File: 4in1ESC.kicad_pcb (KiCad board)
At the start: 6 copper layers, 31.2 x 33 mm, 197 parts, among them J1 SM08B-SRSS-TB, Q1 SP40N03GNJ, Q10 SP40N03GNJ, Q11 SP40N03GNJ, Q12 SP40N03GNJ, Q13 SP40N03GNJ, Q14 SP40N03GNJ, Q15 SP40N03GNJ, Q16 SP40N03GNJ, Q17 SP40N03GNJ, Q18 SP40N03GNJ, Q19 SP40N03GNJ, Q2 SP40N03GNJ, Q20 SP40N03GNJ, Q21 SP40N03GNJ, Q22 SP40N03GNJ, Q23 SP40N03GNJ, Q24 SP40N03GNJ, Q3 SP40N03GNJ, Q4 SP40N03GNJ, Q5 SP40N03GNJ, Q6 SP40N03GNJ, Q7 SP40N03GNJ, Q8 SP40N03GNJ, Q9 SP40N03GNJ, U1 TLV76733DRVR, U10 AT32F421G8U7, U11 NSG2065Q, U12 INA186A3IDCKR, U18 LMR51420YDDCR, U2 AT32F421G8U7, U3 NSG2065Q, U5 XRIM160808SR47MBCD, U6 AT32F421G8U7, U7 NSG2065Q, U8 AT32F421G8U7, U9 NSG2065Q

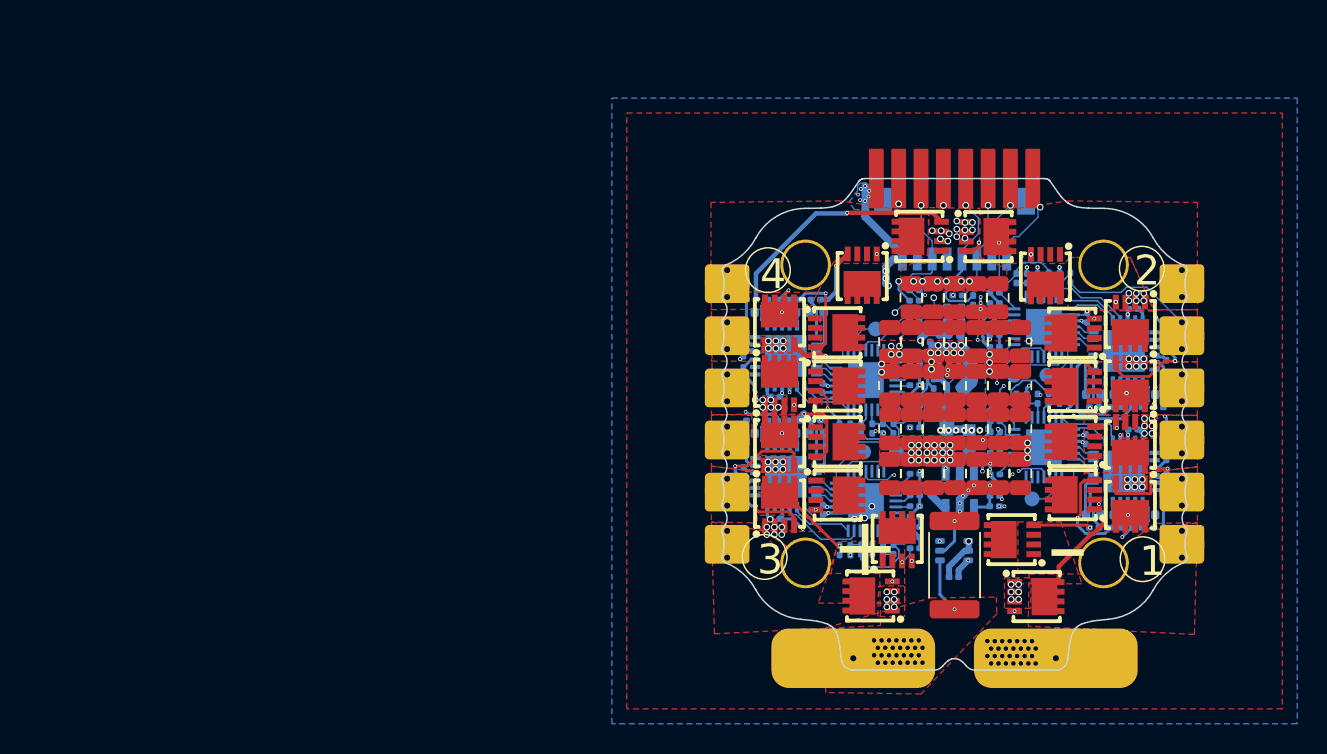
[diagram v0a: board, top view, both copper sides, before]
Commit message: V-beta schematic in progress: buck/inductor/TVS/MOSFET swaps
Stan's V-beta edits via KiCad GUI:
- U13 LMR54406DBVR placed (replacing LMR51420)
- R119 = 115k for 10V output (Vfb=0.8V)
- U5 inductor value updated to FTC160808S4R7MBCA (4.7uH)
- D1 SMF24A-T13 TVS placed across +BATT/GND
- 24x SP40N03GNJ -> DOY180N03T (TDFN3333-8PL)
- 14x bulk caps in 1206 (replacing the 0805 swarm)
- R74 = 10R 0201 added between VDD and VDDA (no ferrite)
- Ferrites FB1-4 removed
- LMR54406 footprint and 3D imported via easyeda2kicad
- SMF24A-T13 footprint and 3D imported via easyeda2kicad

Schematic still has hygiene issues (footprint namespace prefixes,
cap/resistor R/C footprint swaps) to fix in a follow-up.

Generator version bumped to KiCad 10.0 (was 9.x).

Co-Authored-By: Claude Opus 4.7 (1M context) <noreply@anthropic.com>
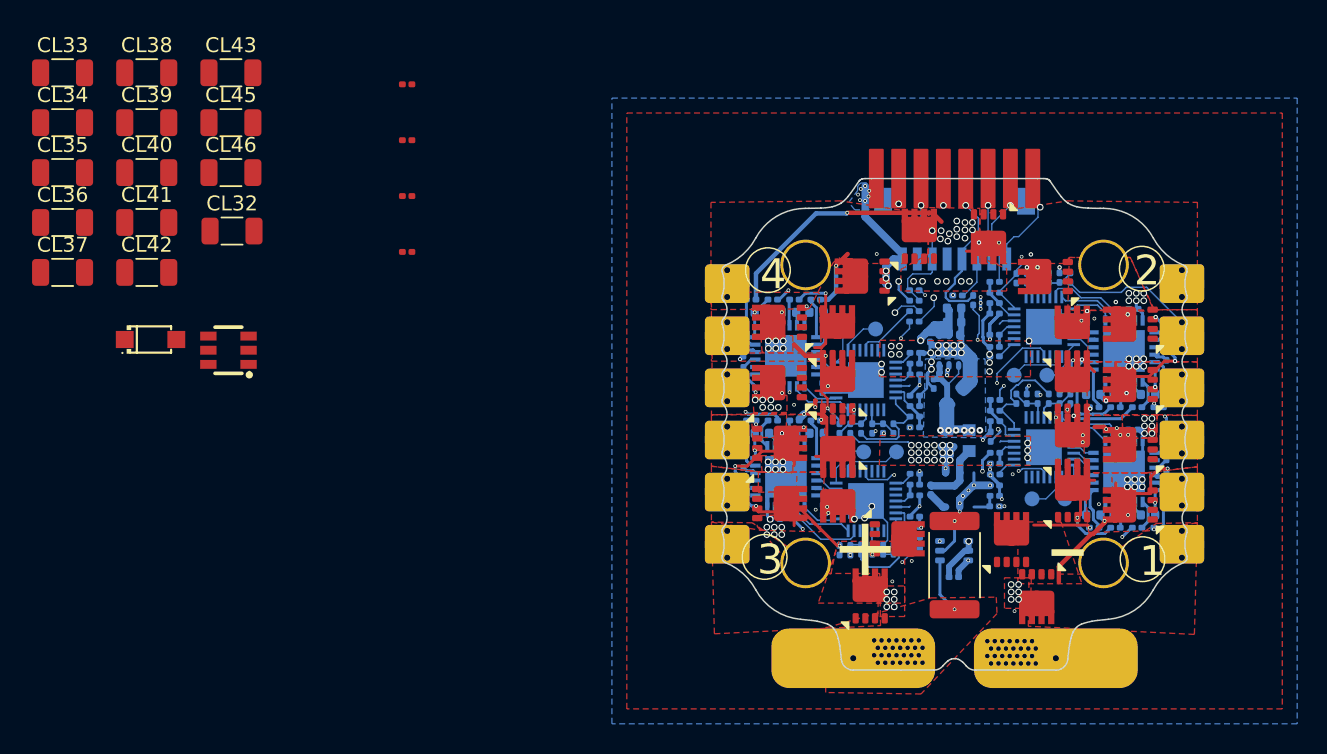
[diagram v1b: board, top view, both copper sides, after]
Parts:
- removed C10, C11, C12, C13, C14, C15, C16, C17, C18, C19, C2, C20, C21, C22, C23, C24, C25, C26, C27, C28, C29, C3, C31, C4, C40, C41, C47, C5, C51, C6, C7, C8, C9: 10uF, Capacitor_SMD:C_0805_2012Metric
- removed FB1, FB2, FB3, FB4: BLM03HD331SN1D, Inductor_SMD:L_0201_0603Metric
- removed U18: LMR51420YDDCR, components:SOT-23-6_L2.9-W1.6-P0.95-LS2.9-BL
- added CL32: 10uF, Capacitor_SMD:C_1206_3216Metric, F.Cu at (27.5, 35.9)
- added CL33: 10uF, Capacitor_SMD:C_1206_3216Metric, F.Cu at (16.1, 25.3)
- added CL34: 10uF, Capacitor_SMD:C_1206_3216Metric, F.Cu at (16.1, 28.6)
- added CL35: 10uF, Capacitor_SMD:C_1206_3216Metric, F.Cu at (16.1, 32.0)
- added CL36: 10uF, Capacitor_SMD:C_1206_3216Metric, F.Cu at (16.1, 35.4)
- added CL37: 10uF, Capacitor_SMD:C_1206_3216Metric, F.Cu at (16.1, 38.7)
- added CL38: 10uF, Capacitor_SMD:C_1206_3216Metric, F.Cu at (21.8, 25.3)
- added CL39: 10uF, Capacitor_SMD:C_1206_3216Metric, F.Cu at (21.8, 28.6)
- added CL40: 10uF, Capacitor_SMD:C_1206_3216Metric, F.Cu at (21.8, 32.0)
- added CL41: 10uF, Capacitor_SMD:C_1206_3216Metric, F.Cu at (21.8, 35.4)
- added CL42: 10uF, Capacitor_SMD:C_1206_3216Metric, F.Cu at (21.8, 38.7)
- added CL43: 10uF, Capacitor_SMD:C_1206_3216Metric, F.Cu at (27.4, 25.3)
- added CL45: 10uF, Capacitor_SMD:C_1206_3216Metric, F.Cu at (27.4, 28.6)
- added CL46: 10uF, Capacitor_SMD:C_1206_3216Metric, F.Cu at (27.4, 32.0)
- added D1: SMF24A-T13, 4in1ESC:SOD-123FL_L2.7-W1.8-LS3.7-RD, F.Cu at (22.0, 43.2)
- added R74: 10R, Resistor_SMD:R_0201_0603Metric, F.Cu at (39.3, 37.3)
- added R75: 10R, Resistor_SMD:R_0201_0603Metric, F.Cu at (39.3, 29.8)
- added R76: 10R, Resistor_SMD:R_0201_0603Metric, F.Cu at (39.3, 33.6)
- added R77: 10R, Resistor_SMD:R_0201_0603Metric, F.Cu at (39.3, 26.1)
- added U13: LMR54406DBVR, 4in1ESC:SOT-23-6_L2.9-W1.6-P0.95-LS2.8-BR, F.Cu at (27.3, 43.9)
- Q1, Q10, Q11, Q12, Q13, Q14, Q15, Q16, Q17, Q18, Q19, Q2, Q20, Q21, Q22, Q23, Q24, Q3, Q4, Q5, Q6, Q7, Q8, Q9: value SP40N03GNJ -> DOY180N03T; footprint components:POWERPAK-1212-8_L3.0-W3.0-P0.65-LS3.3-BL -> Package_SON:Diodes_PowerDI3333-8
- R119: value 124k -> 115k
- U5: value XRIM160808SR47MBCD -> FTC160808S4R7MBCA
- turned Q21 to 90 degrees
- turned Q22 to 180 degrees
- turned Q23 to 90 degrees
- turned Q24 to 180 degrees
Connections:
- net +8V renamed +10V
- C44 pad 1: +3V3 -> /ESC2/vdda
- C48 pad 1: +3V3 -> /ESC1/vdda
- C64 pad 1: +3V3 -> /ESC3/vdda
- C78 pad 1: +3V3 -> /ESC4/vdda
- U10 pad 5: Net-(U10-VDDA) -> /ESC4/vdda
- U2 pad 5: Net-(U2-VDDA) -> /ESC1/vdda
- U6 pad 5: Net-(U6-VDDA) -> /ESC2/vdda
- U8 pad 5: Net-(U8-VDDA) -> /ESC3/vdda
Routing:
- net +10V: track 13.5 -> 11.9 mm, vias 12 -> 10
- net (no net): track 0.00 -> 1.57 mm, vias 0 -> 2
- net Net-(U6-VDDA): track 1.14 -> 0.00 mm
- net /ESC2/vdda: track 0.00 -> 1.14 mm
- net Net-(U8-VDDA): track 0.98 -> 0.00 mm
- net /ESC3/vdda: track 0.00 -> 0.98 mm
- net Net-(U2-VDDA): track 0.98 -> 0.00 mm
- net Net-(U10-VDDA): track 0.98 -> 0.00 mm
- net /ESC4/vdda: track 0.00 -> 0.98 mm
- net /ESC1/vdda: track 0.00 -> 0.98 mm
- net Net-(Q8-G): vias 2 -> 3
- net GND: vias 176 -> 171
- net /ESC3/MotorA: vias 2 -> 4
- net /ESC1/MotorA: vias 2 -> 4
